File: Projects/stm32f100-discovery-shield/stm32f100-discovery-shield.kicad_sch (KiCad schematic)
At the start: 3 parts, among them P1 CONN28, P2 CONN28, P3 CONN6

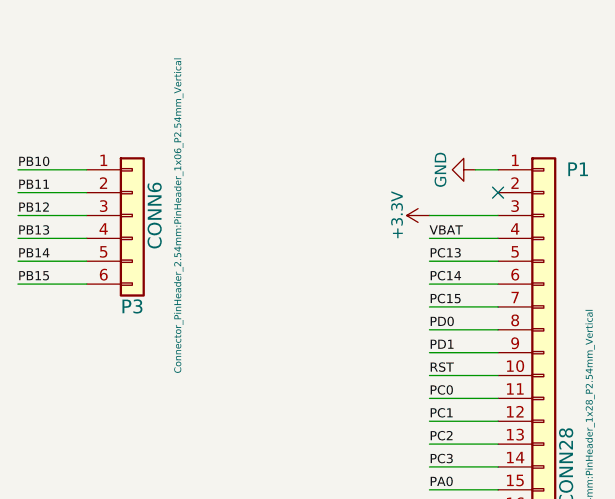
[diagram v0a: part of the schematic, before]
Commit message: Update templates to V8 format
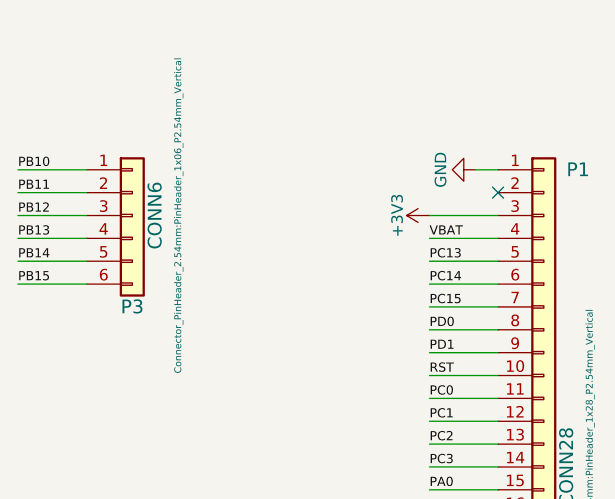
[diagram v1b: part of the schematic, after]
